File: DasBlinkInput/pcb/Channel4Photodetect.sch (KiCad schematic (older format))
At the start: 6 parts, among them P501 TP_CHAN4, U201 MCP6404, U202 LM339

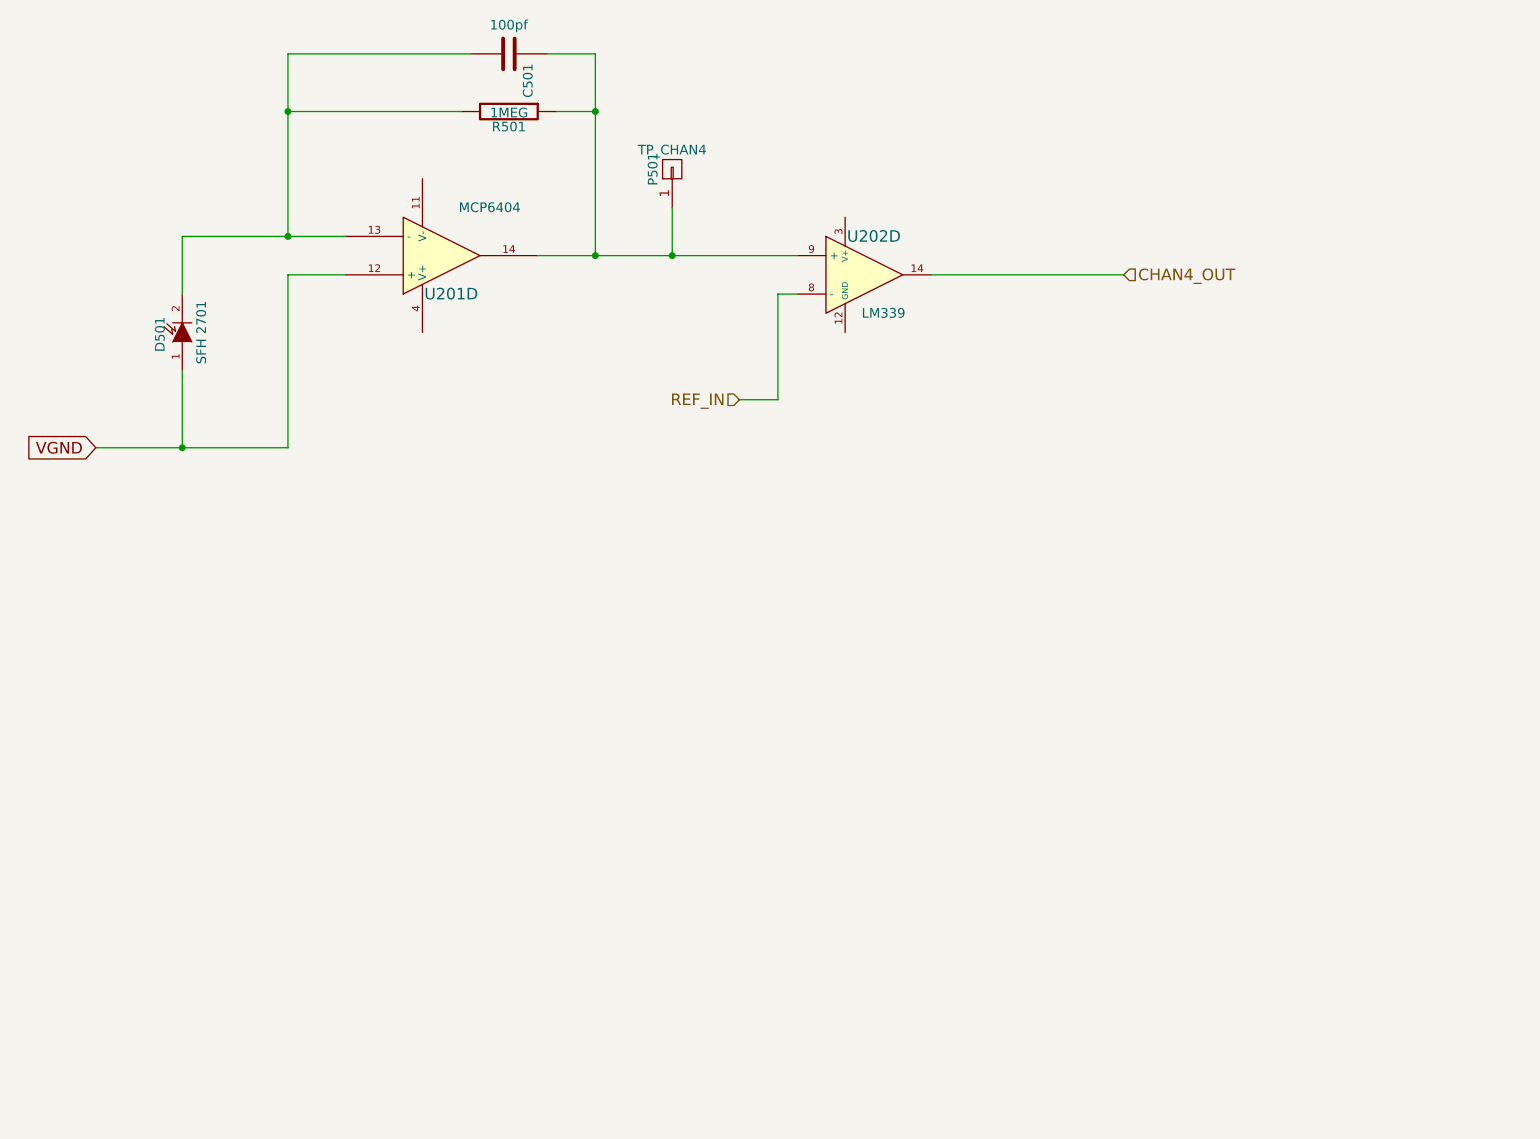
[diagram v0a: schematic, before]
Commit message: DBI - fixed reg/on pin, changed resistor to 0 ohm near divider and rv, added 10k pull up resistors to 3V for each output channel.
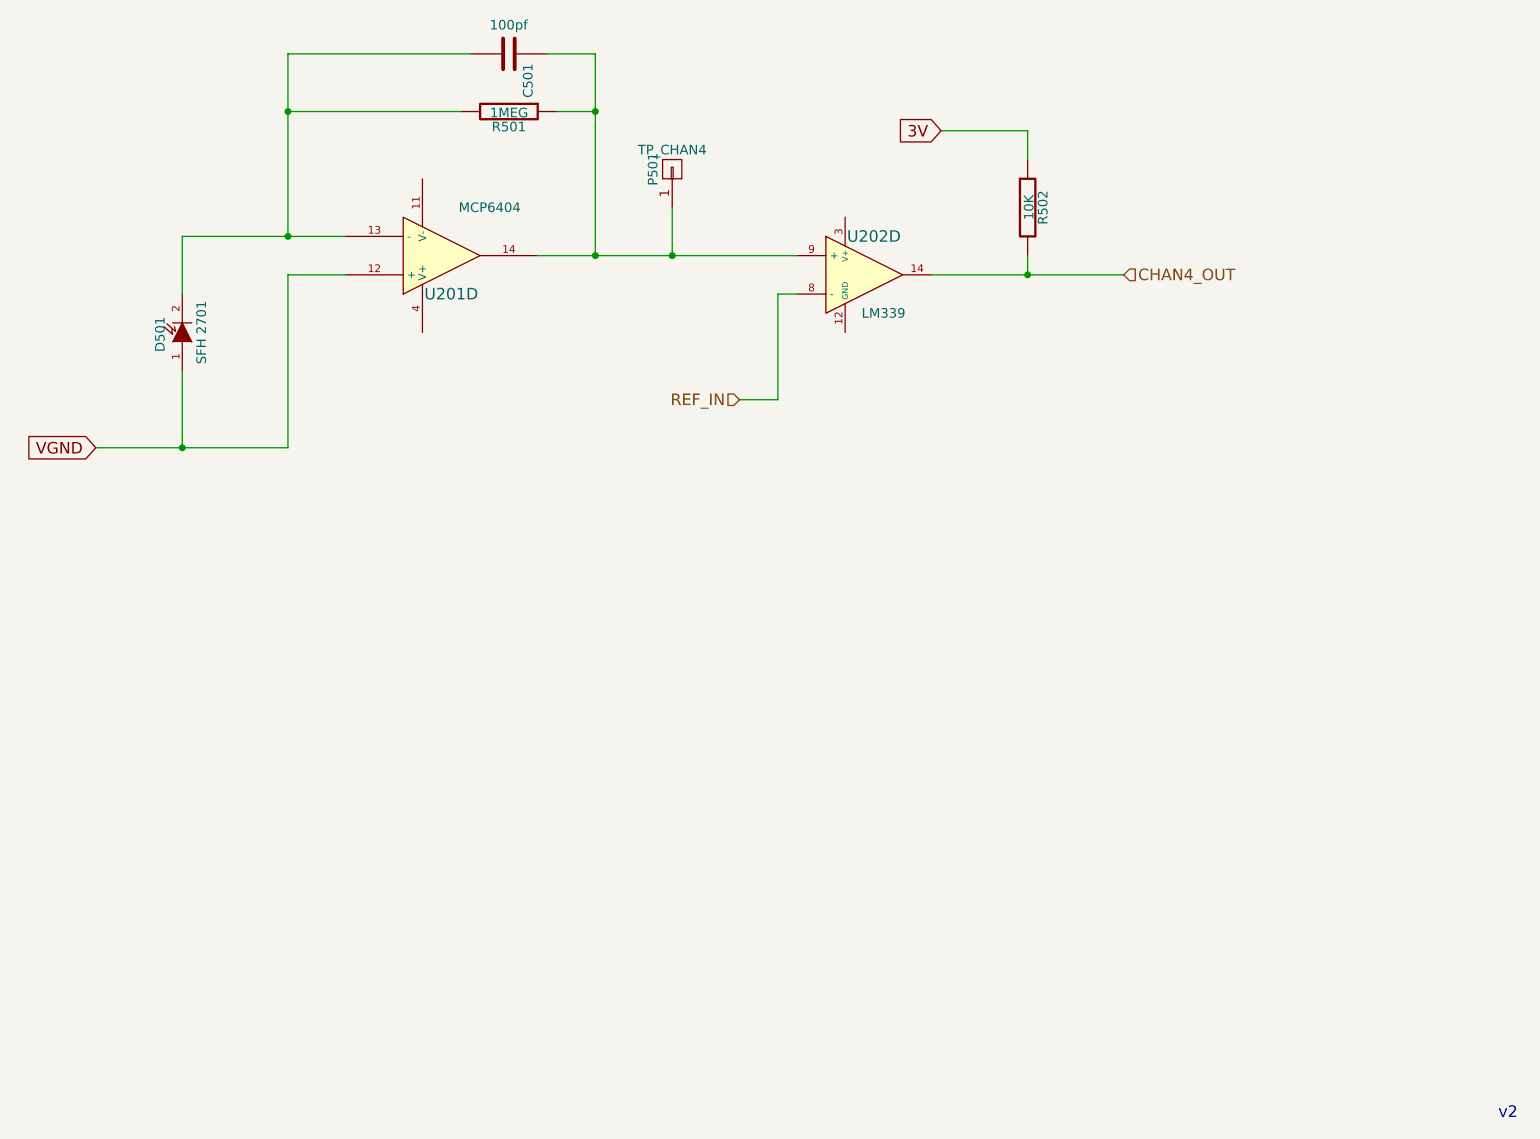
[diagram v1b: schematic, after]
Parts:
- added R502: 10K, Resistors_SMD:R_0805_HandSoldering, symbol R
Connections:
- net CHAN4_OUT: now also R502.2
- new net 3V: R502.1
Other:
- note added: "v2"
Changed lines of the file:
@@
 	6300 2900 6300 3150
 Connection ~ 6300 3150
+Text Notes 10600 7650 0    60   ~ 0
+v2
+$Comp
+L R R502
+U 1 1 55B5A291
+P 8150 2900
+F 0 "R502" V 8230 2900 50  0000 C CNN
+F 1 "10K" V 8157 2901 50  0000 C CNN
+F 2 "Resistors_SMD:R_0805_HandSoldering" V 8080 2900 30  0001 C CNN
+F 3 "" H 8150 2900 30  0000 C CNN
+	1    8150 2900
+	1    0    0    -1
+$EndComp
+Text GLabel 7700 2500 0    60   Input ~ 0
+3V
+Wire Wire Line
+	7700 2500 8150 2500
+Wire Wire Line
+	8150 2500 8150 2650
+Wire Wire Line
+	8150 3150 8150 3250
+Connection ~ 8150 3250
 $EndSCHEMATC
